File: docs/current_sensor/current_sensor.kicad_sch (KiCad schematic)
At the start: 5 parts, among them J1 Connector, U1 LM358

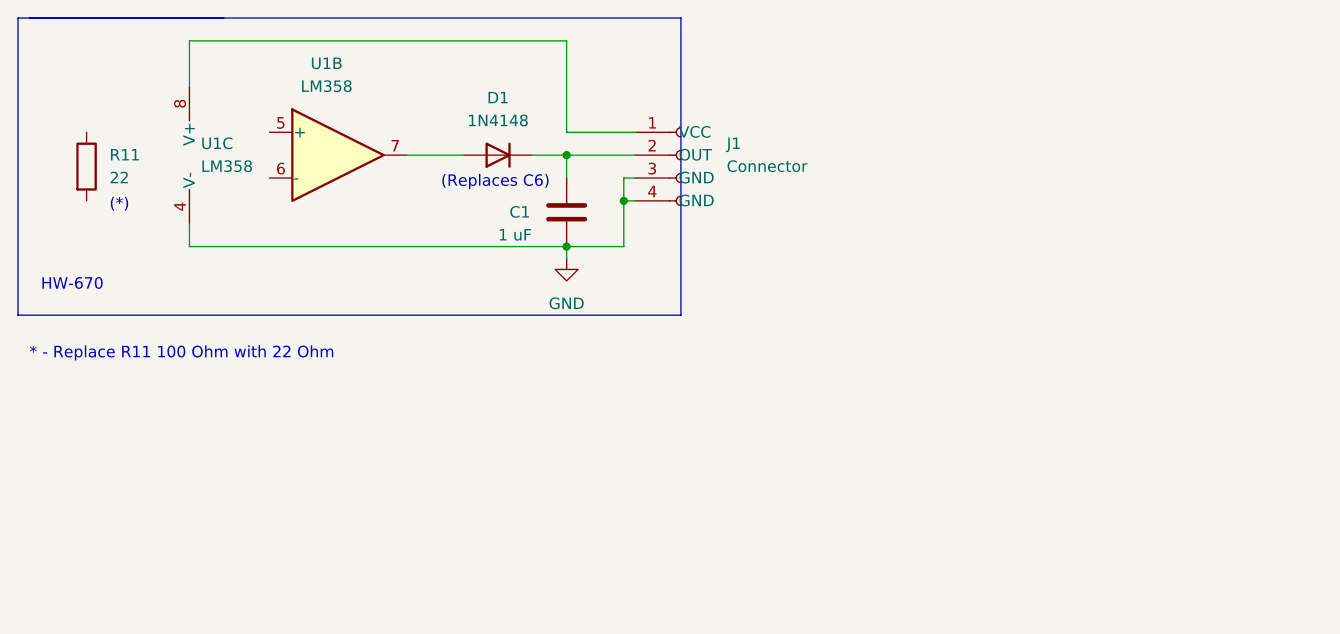
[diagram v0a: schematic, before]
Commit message: Added schematics and pictures regarding the adaptation for the Delba heater.
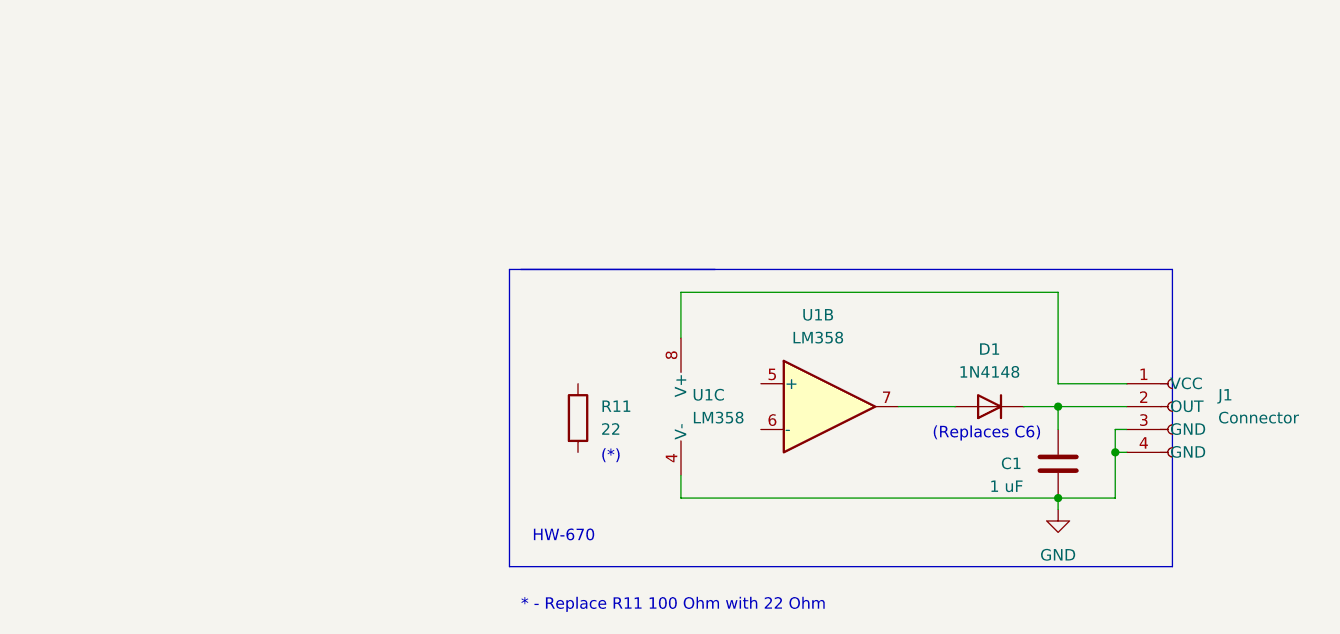
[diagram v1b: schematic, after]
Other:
- moved on the sheet: C1, D1, J1, R11, U1B, U1C
